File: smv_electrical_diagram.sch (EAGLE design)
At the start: 1 part

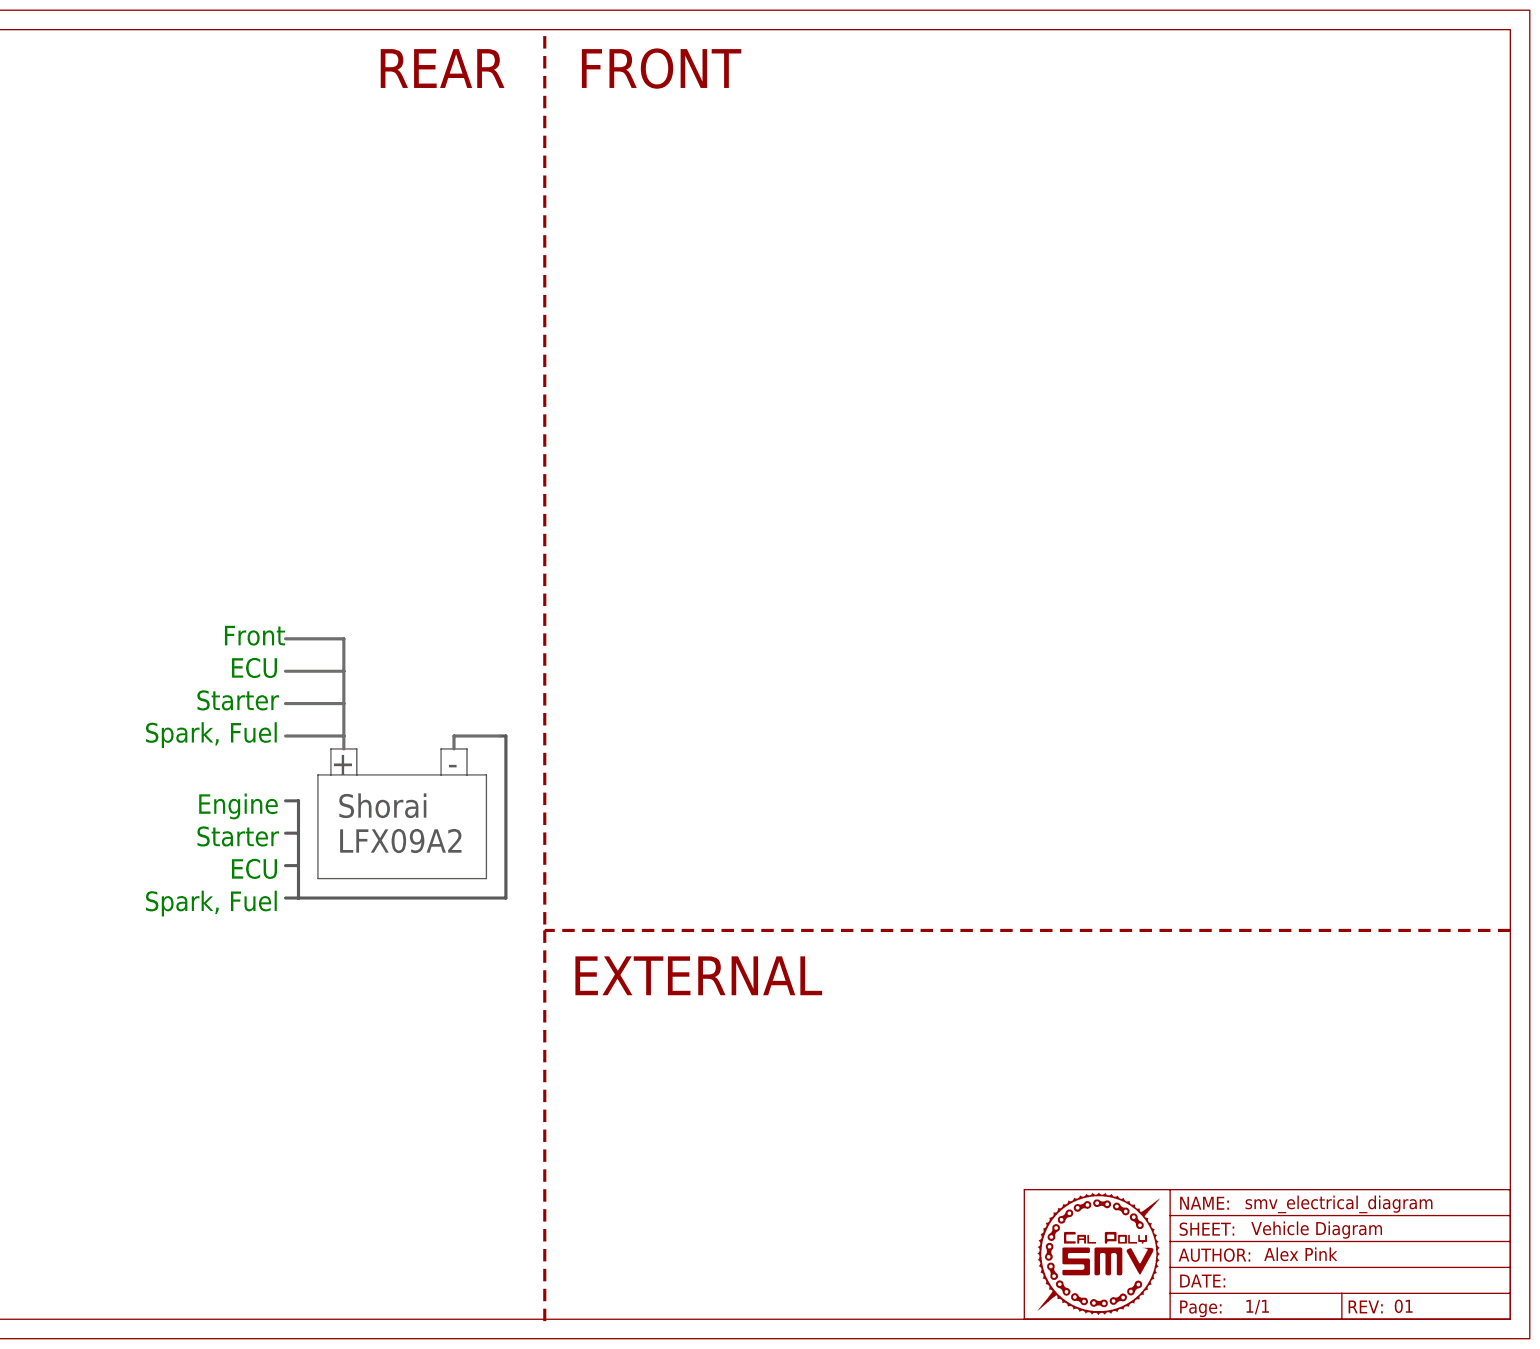
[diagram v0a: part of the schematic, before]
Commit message: Reduced size of test points + other minor changes. Coincides with first efi-shield PCB commit.
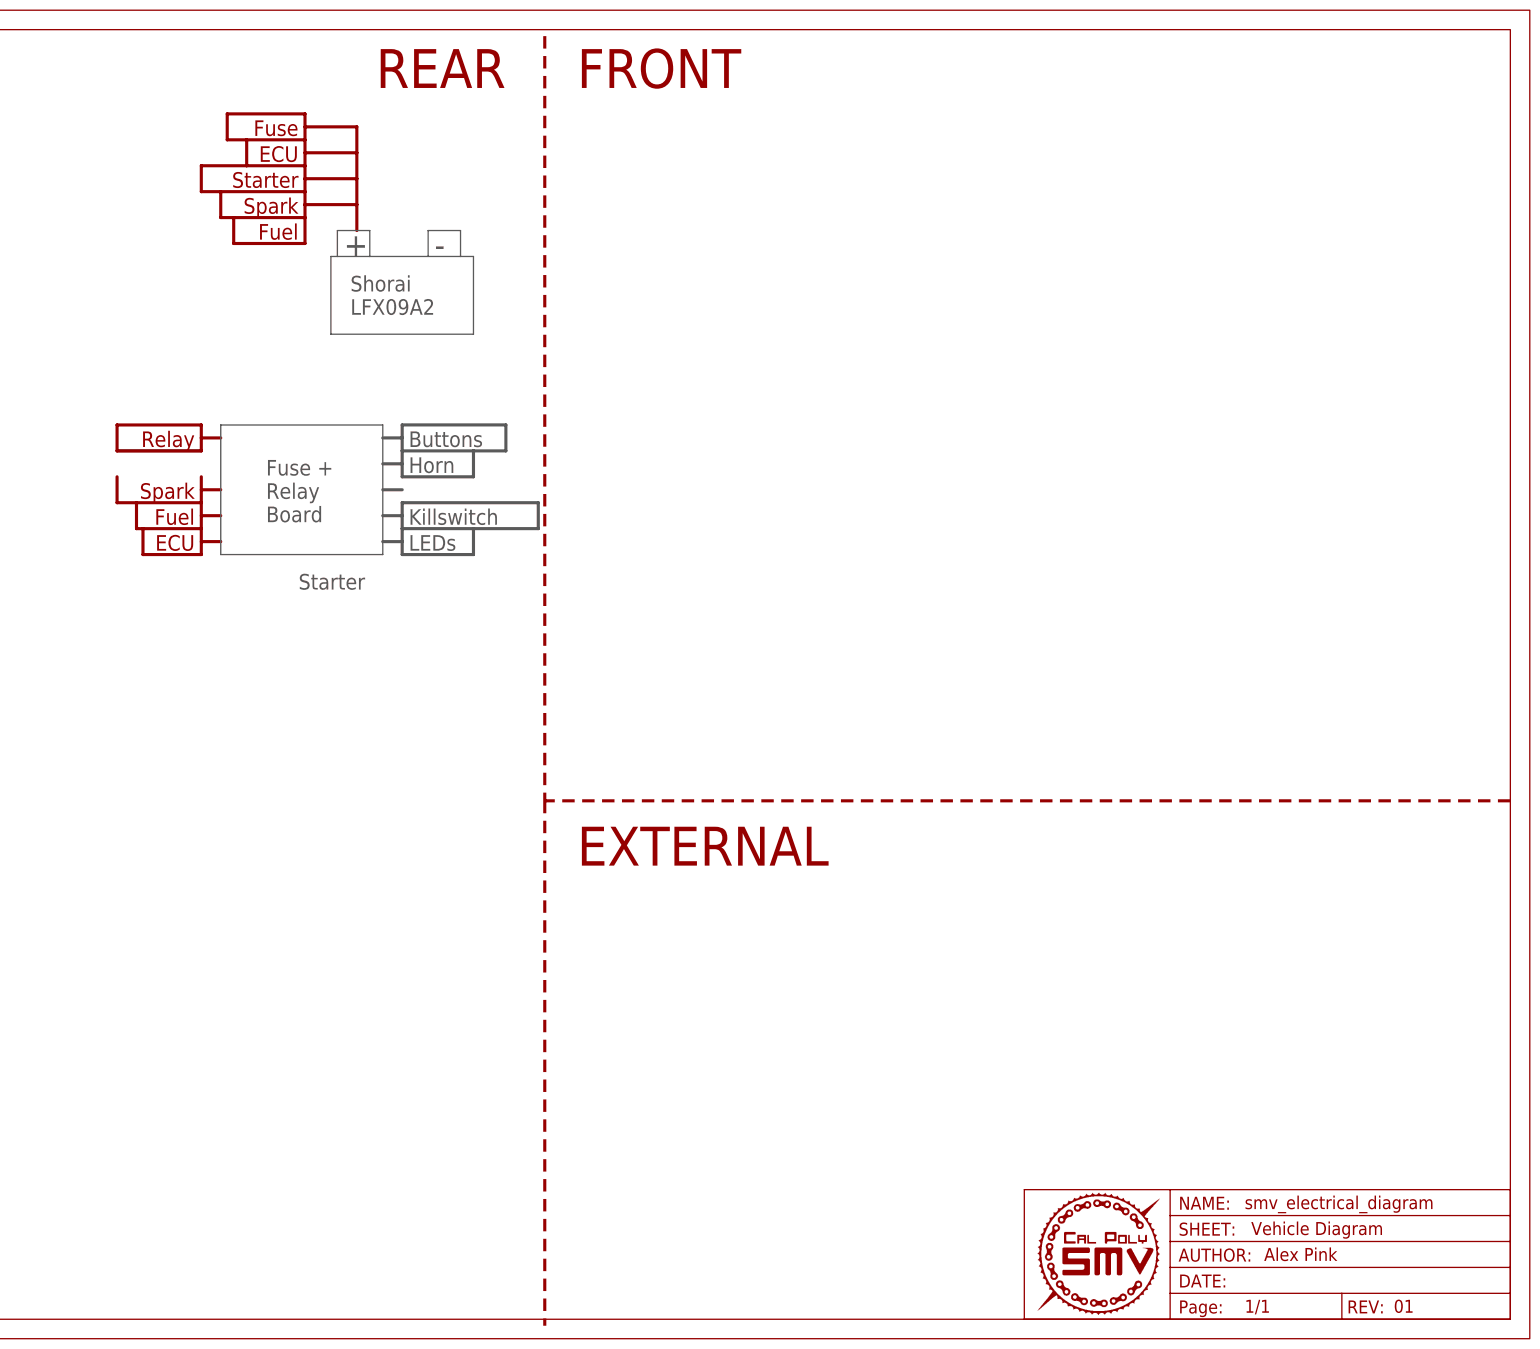
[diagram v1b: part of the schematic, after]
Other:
- note added: "Buttons"
- note added: "Fuel"
- note added: "Fuse"
- note added: "Fuse + Relay Board"
- note added: "Horn"
- note added: "Killswitch"
- note added: "LEDs"
- note added: "Relay"
- note added: "Spark"
- note removed: "Front"
- note removed: "Spark, Fuel"
